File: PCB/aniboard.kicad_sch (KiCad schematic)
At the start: 368 parts, among them J1 Conn_02x03_Top_Bottom, SW1 SW_Push, SW10 SW_Push, SW11 SW_Push, SW12 SW_Push, SW13 SW_Push, SW14 SW_Push, SW15 SW_Push, SW16 SW_Push, SW17 SW_Push, SW18 SW_Push, SW19 SW_Push, SW2 SW_Push, SW20 SW_Push, SW21 SW_Push, SW22 SW_Push, SW23 SW_Push, SW24 SW_Push, SW25 SW_Push, SW26 SW_Push, SW27 SW_Push, SW28 SW_Push, SW29 SW_Push, SW3 SW_Push, SW30 SW_Push, SW31 SW_Push, SW32 SW_Push, SW33 SW_Push, SW34 SW_Push, SW35 SW_Push, SW36 SW_Push, SW37 SW_Push, SW38 SW_Push, SW39 SW_Push, SW4 SW_Push, SW40 SW_Push, SW41 SW_Push, SW42 SW_Push, SW43 SW_Push, SW44 SW_Push, SW45 SW_Push, SW46 SW_Push, SW47 SW_Push, SW48 SW_Push, SW49 SW_Push, SW5 SW_Push, SW50 SW_Push, SW51 SW_Push, SW52 SW_Push, SW53 SW_Push, SW54 SW_Push, SW55 SW_Push, SW56 SW_Push, SW57 SW_Push, SW58 SW_Push, SW59 SW_Push, SW6 SW_Push, SW60 SW_Push, SW61 SW_Push, SW62 SW_Push, SW63 SW_Push, SW64 SW_Push, SW65 SW_Push, SW66 SW_Push, SW67 SW_Push, SW68 SW_Push, SW69 SW_Push, SW7 SW_Push, SW70 SW_Push, SW71 SW_Push, SW72 SW_Push, SW73 SW_Push, SW74 SW_Push, SW75 SW_Push, SW76 SW_Push, SW77 SW_Push, SW78 SW_Push, SW79 SW_Push, SW8 SW_Push, SW80 SW_Push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

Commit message: Half done with routing
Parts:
- removed JP1: SolderJumper_2_Bridged, Jumper:SolderJumper-2_P1.3mm_Bridged_RoundedPad1.0x1.5mm, symbol Jumper:SolderJumper_2_Bridged
- removed JP2: SolderJumper_2_Open, Jumper:SolderJumper-2_P1.3mm_Open_RoundedPad1.0x1.5mm, symbol Jumper:SolderJumper_2_Open
- added C91, C92: 0.1uf, Capacitor_SMD:C_0805_2012Metric_Pad1.18x1.45mm_HandSolder, symbol Device:C_Small
- added R2: 470Ω, Resistor_SMD:R_0805_2012Metric_Pad1.20x1.40mm_HandSolder, symbol Device:R
- added R3: 100Ω, Resistor_SMD:R_0805_2012Metric_Pad1.20x1.40mm_HandSolder, symbol Device:R
- D89: value LED -> Blue LED; footprint (none) -> LED_SMD:LED_0603_1608Metric_Pad1.05x0.95mm_HandSolder
- D90: value LED -> Green LED; footprint (none) -> LED_SMD:LED_0603_1608Metric_Pad1.05x0.95mm_HandSolder
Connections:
- net +3.3V: now also U2.6 (VCCB), C91.2; no longer U2.1 (VCCA), U2.5 (DIR)
- net +5V: now also U1.39 (VSYS), U1.40 (VBUS), U2.1 (VCCA), C92.1, R2.1; no longer U2.6 (VCCB)
- net COL0: now also U1.21 (GPIO16); no longer U1.34 (GPIO28_ADC2)
- net COL1: now also U1.22 (GPIO17); no longer U1.32 (GPIO27_ADC1)
- net COL10: now also U1.17 (GPIO13); no longer U1.14 (GPIO10)
- net COL11: now also U1.19 (GPIO14); no longer U1.15 (GPIO11)
- net COL12: now also U1.15 (GPIO11); no longer U1.16 (GPIO12)
- net COL13: now also U1.14 (GPIO10)
- net COL14: now also U1.12 (GPIO9); no longer U1.10 (GPIO7)
- net COL15: now also U1.11 (GPIO8); no longer U1.9 (GPIO6)
- net COL16: now also U1.7 (GPIO5); no longer U1.5 (GPIO3)
- net COL2: now also U1.24 (GPIO18); no longer U1.22 (GPIO17)
- net COL3: now also U1.25 (GPIO19); no longer U1.20 (GPIO15)
- net COL4: now also U1.26 (GPIO20)
- net COL5: now also U1.27 (GPIO21)
- net COL6: now also U1.29 (GPIO22)
- net COL7: now also U1.31 (GPIO26_ADC0)
- net COL8: now also U1.32 (GPIO27_ADC1); no longer U1.11 (GPIO8)
- net COL9: now also U1.16 (GPIO12); no longer U1.12 (GPIO9)
- net GND: now also D89.1 (K), D90.1 (K), U2.5 (DIR), C91.1, C92.2; no longer U1.23 (GND)
- net LED: now also U1.34 (GPIO28_ADC2), U2.4 (B); no longer U1.21 (GPIO16), U2.3 (A)
- net ROW0: now also U1.20 (GPIO15); no longer U1.31 (GPIO26_ADC0)
- net ROW4: now also U1.10 (GPIO7); no longer U1.7 (GPIO5)
- net ROW5: now also U1.9 (GPIO6); no longer U1.6 (GPIO4)
- net RX: now also U1.6 (GPIO4)
- net TX: now also U1.5 (GPIO3)
- net at JP3.1 (A), R1.2: now also U2.3 (A); no longer U2.4 (B)
- net at D90.2 (A): now also R3.2
- net at D89.2 (A): now also R2.2
- new net INDICATOR: R3.1
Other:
- note added: "Indicator LEDs"
- moved on the sheet: D89, D90, U2

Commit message: Finish routing
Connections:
- net ROW0 is gone; now on net INDICATOR: D1.1 (K), D10.1 (K), D11.1 (K), D12.1 (K), D13.1 (K), D14.1 (K), D2.1 (K), D3.1 (K), D4.1 (K), D5.1 (K), D6.1 (K), D7.1 (K), D8.1 (K), D9.1 (K), U1.20 (GPIO15)
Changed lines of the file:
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@@
+		)
+	)
+	(global_label "INDICATOR"
+		(shape input)
+		(at 410.21 223.52 270)
+		(fields_autoplaced yes)
+		(effects
+			(font
+				(size 1.27 1.27)
+			)
+			(justify right)
+		)
+		(property "Intersheetrefs" "${INTERSHEET_REFS}"
+			(at 410.21 236.242 90)
+			(effects
+				(font
+					(size 1.27 1.27)
+				)
+				(justify right)
+				(hide yes)
+			)
 		)
 	)

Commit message: V1.2
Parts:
- removed J1: Conn_02x03_Top_Bottom, Connector_PinHeader_2.54mm:PinHeader_2x03_P2.54mm_Vertical, symbol Connector_Generic:Conn_02x03_Top_Bottom
- added Brd1: SSD1306, OLED:SSD1306-0.91-OLED-4pin-128x32, symbol OLED:SSD1306
- added C93: 1uf, Capacitor_SMD:C_0805_2012Metric_Pad1.18x1.45mm_HandSolder, symbol Device:C_Small
- added H1: MountingHole_Pad, MountingHole:MountingHole_3.2mm_M3_Pad_Via, symbol Mechanical:MountingHole_Pad
- added J2: Conn_01x03_Pin, Connector_PinHeader_2.54mm:PinHeader_1x03_P2.54mm_Vertical, symbol Connector:Conn_01x03_Pin
- added R4, R5: 4.7kΩ, Resistor_SMD:R_0805_2012Metric_Pad1.20x1.40mm_HandSolder, symbol Device:R
- C89, C90: value 500uf -> 5uf; footprint Capacitor_THT:CP_Radial_D8.0mm_P3.50mm -> Capacitor_THT:CP_Radial_D6.3mm_P2.50mm
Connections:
- net TX is gone; now on net COL16: U1.5 (GPIO3)
- net +3.3V: now also R4.1, R5.1
- net +5V: now also Brd1.2 (VCC), C93.2
- net COL10: now also U1.16 (GPIO12); no longer U1.17 (GPIO13)
- net COL11: now also U1.17 (GPIO13); no longer U1.19 (GPIO14)
- net COL12: now also U1.19 (GPIO14); no longer U1.15 (GPIO11)
- net COL16: no longer U1.7 (GPIO5)
- net COL9: now also U1.15 (GPIO11); no longer U1.16 (GPIO12)
- net GND: now also U1.23 (GND), Brd1.1 (GND), C93.1, H1.1, J2.2 (Pin_2)
- net at U1.41 (SWCLK): now also J2.1 (Pin_1)
- net at U1.43 (SWDIO): now also J2.3 (Pin_3)
- net RX: no longer names the net of U1.6 (GPIO4)
- net RX: now also Brd1.4 (SDA), R5.2
- new net: Brd1.3 (SCL), R4.2, U1.7 (GPIO5)

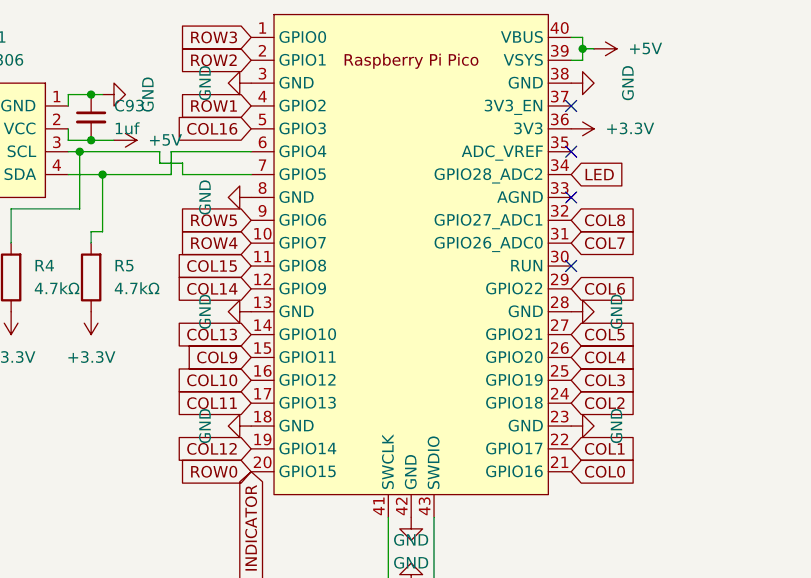
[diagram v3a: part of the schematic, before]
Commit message: Reroute and silkscreen
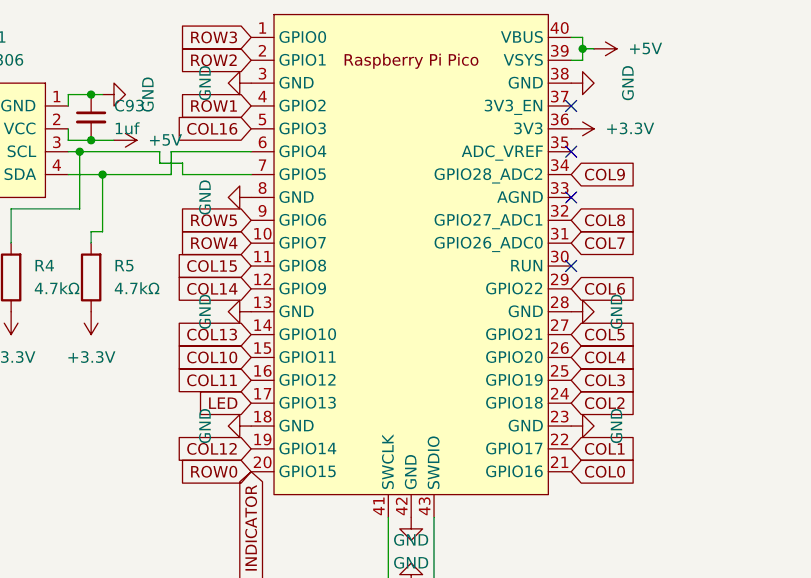
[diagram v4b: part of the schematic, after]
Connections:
- net COL10: now also U1.15 (GPIO11); no longer U1.16 (GPIO12)
- net COL11: now also U1.16 (GPIO12); no longer U1.17 (GPIO13)
- net COL9: now also U1.34 (GPIO28_ADC2); no longer U1.15 (GPIO11)
- net LED: now also U1.17 (GPIO13); no longer U1.34 (GPIO28_ADC2)

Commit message: Last pass
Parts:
- removed H1: MountingHole_Pad, MountingHole:MountingHole_3.2mm_M3_Pad_Via, symbol Mechanical:MountingHole_Pad
- D1, D10, D11, D12, D13, D14, D15, D16, D17, D18, D19, D2, D20, D21, D22, D23, D24, D25, D26, D27, D28, D29, D3, D30, D31, D32, D33, D34, D35, D36, D37, D38, D39, D4, D40, D41, D42, D43, D44, D45, D46, D47, D48, D49, D5, D50, D51, D52, D53, D54, D55, D56, D57, D58, D59, D6, D60, D61, D62, D63, D64, D65, D66, D67, D68, D69, D7, D70, D71, D72, D73, D74, D75, D76, D77, D78, D79, D8, D80, D81, D82, D83, D84, D85, D86, D87, D88, D9: footprint Diode_SMD:D_MiniMELF_Handsoldering -> Library:D_MiniMELF_Handsoldering

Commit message: Save
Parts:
- added J1, J2: USB_C_Receptacle_PowerOnly_24P, Connector_USB:USB_C_Receptacle_GCT_USB4135-GF-A_6P_TopMnt_Horizontal, symbol Connector:USB_C_Receptacle_PowerOnly_24P
- added J3, J4: Conn_01x02_Pin, Connector_PinHeader_2.54mm:PinHeader_1x02_P2.54mm_Vertical, symbol Connector:Conn_01x02_Pin
- added R6, R7, R8, R9: 5.1kΩ, Resistor_SMD:R_0805_2012Metric_Pad1.20x1.40mm_HandSolder, symbol Device:R
- C89, C90: value 5uf -> 4.7uf
- renumbered J2 to J5
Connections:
- net +5V: no longer C15.1, C16.1, C17.1, C18.1, C19.1, C20.1, C21.1, C22.1, C23.1, C24.1, C25.1, C26.1, C27.1, C28.1, C29.1, C30.1, C31.1, C32.1, C33.1, C34.1, C35.1, C36.1, C37.1, C38.1, C39.1, C40.1, C41.1, C42.1, C43.1, C44.1, C45.1, C46.1, C47.1, C48.1, C49.1, C50.1, C51.1, C52.1, C53.1, C54.1, C55.1, C56.1, C57.1, C58.1, C59.1, C60.1, C61.1, C62.1, C63.1, C64.1, C65.1, C66.1, C67.1, C68.1, C69.1, C70.1, C71.1, C72.1, C73.1, C74.1, C75.1, C76.1, C77.1, C78.1, C79.1, C80.1, C81.1, C82.1, C83.1, C84.1, C85.1, C86.1, C87.1, C88.1, LED15.1 (VDD), LED16.1 (VDD), LED17.1 (VDD), LED18.1 (VDD), LED19.1 (VDD), LED20.1 (VDD), LED21.1 (VDD), LED22.1 (VDD), LED23.1 (VDD), LED24.1 (VDD), LED25.1 (VDD), LED26.1 (VDD), LED27.1 (VDD), LED28.1 (VDD), LED29.1 (VDD), LED30.1 (VDD), LED31.1 (VDD), LED32.1 (VDD), LED33.1 (VDD), LED34.1 (VDD), LED35.1 (VDD), LED36.1 (VDD), LED37.1 (VDD), LED38.1 (VDD), LED39.1 (VDD), LED40.1 (VDD), LED41.1 (VDD), LED42.1 (VDD), LED43.1 (VDD), LED44.1 (VDD), LED45.1 (VDD), LED46.1 (VDD), LED47.1 (VDD), LED48.1 (VDD), LED49.1 (VDD), LED50.1 (VDD), LED51.1 (VDD), LED52.1 (VDD), LED53.1 (VDD), LED54.1 (VDD), LED55.1 (VDD), LED56.1 (VDD), LED57.1 (VDD), LED58.1 (VDD), LED59.1 (VDD), LED60.1 (VDD), LED61.1 (VDD), LED62.1 (VDD), LED63.1 (VDD), LED64.1 (VDD), LED65.1 (VDD), LED66.1 (VDD), LED67.1 (VDD), LED68.1 (VDD), LED69.1 (VDD), LED70.1 (VDD), LED71.1 (VDD), LED72.1 (VDD), LED73.1 (VDD), LED74.1 (VDD), LED75.1 (VDD), LED76.1 (VDD), LED77.1 (VDD), LED78.1 (VDD), LED79.1 (VDD), LED80.1 (VDD), LED81.1 (VDD), LED82.1 (VDD), LED83.1 (VDD), LED84.1 (VDD), LED85.1 (VDD), LED86.1 (VDD), LED87.1 (VDD), LED88.1 (VDD)
- net GND: now also J1.A1 (GND), J1.A12 (GND), J1.B1 (GND), J1.B12 (GND), J2.A1 (GND), J2.A12 (GND), J2.B1 (GND), J2.B12 (GND), J3.2 (Pin_2), J4.2 (Pin_2), R6.2, R7.2, R8.2, R9.2
- net INDICATOR renamed ROW0
- new net: J2.A5 (CC1), R8.1
- new net: J2.B5 (CC2), R9.1
- new net: J1.A5 (CC1), R6.1
- new net: J1.B5 (CC2), R7.1
- new net +5VA: C15.1, C16.1, C17.1, C18.1, C19.1, C20.1, C21.1, C22.1, C23.1, C24.1, C25.1, C26.1, C27.1, C28.1, C29.1, C30.1, C31.1, C32.1, C33.1, C34.1, C35.1, C36.1, C37.1, C38.1, C39.1, C40.1, C41.1, C42.1, C80.1, C81.1, C82.1, C83.1, C84.1, C85.1, J1.A4 (VBUS), J1.A9 (VBUS), J1.B4 (VBUS), J1.B9 (VBUS), J3.1 (Pin_1), LED15.1 (VDD), LED16.1 (VDD), LED17.1 (VDD), LED18.1 (VDD), LED19.1 (VDD), LED20.1 (VDD), LED21.1 (VDD), LED22.1 (VDD), LED23.1 (VDD), LED24.1 (VDD), LED25.1 (VDD), LED26.1 (VDD), LED27.1 (VDD), LED28.1 (VDD), LED29.1 (VDD), LED30.1 (VDD), LED31.1 (VDD), LED32.1 (VDD), LED33.1 (VDD), LED34.1 (VDD), LED35.1 (VDD), LED36.1 (VDD), LED37.1 (VDD), LED38.1 (VDD), LED39.1 (VDD), LED40.1 (VDD), LED41.1 (VDD), LED42.1 (VDD), LED80.1 (VDD), LED81.1 (VDD), LED82.1 (VDD), LED83.1 (VDD), LED84.1 (VDD), LED85.1 (VDD)
- new net +5VB: C43.1, C44.1, C45.1, C46.1, C47.1, C48.1, C49.1, C50.1, C51.1, C52.1, C53.1, C54.1, C55.1, C56.1, C57.1, C58.1, C59.1, C60.1, C61.1, C62.1, C63.1, C64.1, C65.1, C66.1, C67.1, C68.1, C69.1, C70.1, C71.1, C72.1, C73.1, C74.1, C75.1, C76.1, C77.1, C78.1, C79.1, C86.1, C87.1, C88.1, J2.A4 (VBUS), J2.A9 (VBUS), J2.B4 (VBUS), J2.B9 (VBUS), J4.1 (Pin_1), LED43.1 (VDD), LED44.1 (VDD), LED45.1 (VDD), LED46.1 (VDD), LED47.1 (VDD), LED48.1 (VDD), LED49.1 (VDD), LED50.1 (VDD), LED51.1 (VDD), LED52.1 (VDD), LED53.1 (VDD), LED54.1 (VDD), LED55.1 (VDD), LED56.1 (VDD), LED57.1 (VDD), LED58.1 (VDD), LED59.1 (VDD), LED60.1 (VDD), LED61.1 (VDD), LED62.1 (VDD), LED63.1 (VDD), LED64.1 (VDD), LED65.1 (VDD), LED66.1 (VDD), LED67.1 (VDD), LED68.1 (VDD), LED69.1 (VDD), LED70.1 (VDD), LED71.1 (VDD), LED72.1 (VDD), LED73.1 (VDD), LED74.1 (VDD), LED75.1 (VDD), LED76.1 (VDD), LED77.1 (VDD), LED78.1 (VDD), LED79.1 (VDD), LED86.1 (VDD), LED87.1 (VDD), LED88.1 (VDD)
- no-connect marks 5 -> 7

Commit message: Dual USB powah
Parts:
- removed J2: USB_C_Receptacle_PowerOnly_24P, Connector_USB:USB_C_Receptacle_GCT_USB4135-GF-A_6P_TopMnt_Horizontal, symbol Connector:USB_C_Receptacle_PowerOnly_24P
- removed R8: 5.1kΩ, Resistor_SMD:R_0805_2012Metric_Pad1.20x1.40mm_HandSolder, symbol Device:R
- added C100, C105, C36, C72: 10nF, Capacitor_SMD:C_0402_1005Metric_Pad0.74x0.62mm_HandSolder, symbol Device:C
- added C101, C106, C37, C73: 400pF, Capacitor_SMD:C_0402_1005Metric_Pad0.74x0.62mm_HandSolder, symbol Device:C
- added C104, C18, C55, C98: 0.1uF, Capacitor_SMD:C_0402_1005Metric_Pad0.74x0.62mm_HandSolder, symbol Device:C
- added C17: 4.7uf, Capacitor_THT:CP_Radial_D6.3mm_P2.50mm, symbol Device:C_Polarized
- added D15, D66, D91, D92: LED, LED_SMD:LED_0603_1608Metric_Pad1.05x0.95mm_HandSolder, symbol Device:LED
- added J3: USB_C_Receptacle_PowerOnly_24P, Connector_USB:USB_C_Receptacle_GCT_USB4135-GF-A_6P_TopMnt_Horizontal, symbol Connector:USB_C_Receptacle_PowerOnly_24P
- added JP1, JP3: Jumper_2_Open, Jumper:SolderJumper-2_P1.3mm_Open_RoundedPad1.0x1.5mm, symbol Jumper:Jumper_2_Open
- added P1, P2, P3, P4: ~, Library:TPS25947xx, symbol Library:TPS25947xx
- added R1, R15, R16, R18, R19, R2, R35, R36: 4.7kΩ, Resistor_SMD:R_0402_1005Metric_Pad0.72x0.64mm_HandSolder, symbol Device:R
- added R10, R14, R28, R34: 220Ω, Resistor_SMD:R_0402_1005Metric_Pad0.72x0.64mm_HandSolder, symbol Device:R
- added R11, R17, R29, R37: 1kΩ, Resistor_SMD:R_0402_1005Metric_Pad0.72x0.64mm_HandSolder, symbol Device:R
- added R12, R13, R20, R23, R26, R3, R32, R33, R6: 10kΩ, Resistor_SMD:R_0402_1005Metric_Pad0.72x0.64mm_HandSolder, symbol Device:R
- added R21, R22, R4, R5: 100kΩ, Resistor_SMD:R_0402_1005Metric_Pad0.72x0.64mm_HandSolder, symbol Device:R
- added R24, R25: 5.1kΩ, Resistor_SMD:R_0805_2012Metric_Pad1.20x1.40mm_HandSolder, symbol Device:R
- D93: renamed from D89; value Blue LED -> LED
- D94: renamed from D90; value Green LED -> LED
- R39: renamed from R3; value 100Ω -> 470Ω
- R9: value 5.1kΩ -> 10kΩ; footprint Resistor_SMD:R_0805_2012Metric_Pad1.20x1.40mm_HandSolder -> Resistor_SMD:R_0402_1005Metric_Pad0.72x0.64mm_HandSolder
- S5: footprint PCM_marbastlib-mx:STAB_MX_6.25u -> PCM_marbastlib-mx:STAB_MX_P_6.25u
- renumbered C92 to C102, C91 to C103, C89 to C15, C90 to C16, C15 to C19, C16 to C20, C17 to C21, C18 to C22, C19 to C23, C20 to C24, C21 to C25, C22 to C26, C23 to C27, C24 to C28, C25 to C29, C26 to C30, C27 to C31, C28 to C32, C80 to C33, C81 to C34, C82 to C35, C29 to C38, C30 to C39, C31 to C40, C32 to C41, C33 to C42, C34 to C43, C35 to C44, C36 to C45, C37 to C46, C38 to C47, C39 to C48, C40 to C49, C41 to C50, C42 to C51, C83 to C52, C84 to C53, C85 to C54, C43 to C56, C44 to C57, C45 to C58, C46 to C59, C47 to C60, C48 to C61, C49 to C62, C50 to C63, C51 to C64, C52 to C65, C53 to C66, C54 to C67, C55 to C68, C86 to C69, C87 to C70, C88 to C71, C56 to C74, C57 to C75, C58 to C76, C59 to C77, C60 to C78, C61 to C79, C62 to C80, C63 to C81, C64 to C82, C65 to C83, C66 to C84, C67 to C85, C79 to C86, C68 to C87, C69 to C88, C70 to C89, C71 to C90, C72 to C91, C73 to C92, C74 to C93, C75 to C94, C76 to C95, C77 to C96, C78 to C97, C93 to C99, D15 to D16, D16 to D17, D17 to D18, D18 to D19, D19 to D20, D20 to D21, D21 to D22, D22 to D23, D23 to D24, D24 to D25, D25 to D26, D26 to D27, D27 to D28, D28 to D29, D80 to D30, D81 to D31, D82 to D32, D29 to D33, D30 to D34, D31 to D35, D32 to D36, D33 to D37, D34 to D38, D35 to D39, D36 to D40, D37 to D41, D38 to D42, D39 to D43, D40 to D44, D41 to D45, D42 to D46, D83 to D47, D84 to D48, D85 to D49, D43 to D50, D44 to D51, D45 to D52, D46 to D53, D47 to D54, D48 to D55, D49 to D56, D50 to D57, D51 to D58, D52 to D59, D53 to D60, D54 to D61, D55 to D62, D86 to D63, D87 to D64, D88 to D65, D56 to D67, D57 to D68, D58 to D69, D59 to D70, D60 to D71, D61 to D72, D62 to D73, D63 to D74, D64 to D75, D65 to D76, D66 to D77, D67 to D78, D68 to D80, D69 to D81, D70 to D82, D71 to D83, D72 to D84, D73 to D85, D74 to D86, D75 to D87, D76 to D88, D77 to D89, D78 to D90, J3 to J2, JP3 to JP2, LED80 to LED29, LED81 to LED30, LED82 to LED31, LED29 to LED32, LED30 to LED33, LED31 to LED34, LED32 to LED35, LED33 to LED36, LED34 to LED37, LED35 to LED38, LED36 to LED39, LED37 to LED40, LED38 to LED41, LED39 to LED42, LED40 to LED43, LED41 to LED44, LED42 to LED45, LED83 to LED46, LED84 to LED47, LED85 to LED48, LED43 to LED49, LED44 to LED50, LED45 to LED51, LED46 to LED52, LED47 to LED53, LED48 to LED54, LED49 to LED55, LED50 to LED56, LED51 to LED57, LED52 to LED58, LED53 to LED59, LED54 to LED60, LED55 to LED61, LED86 to LED62, LED87 to LED63, LED88 to LED64, LED56 to LED65, LED57 to LED66, LED58 to LED67, LED59 to LED68, LED60 to LED69, LED61 to LED70, LED62 to LED71, LED63 to LED72, LED64 to LED73, LED65 to LED74, LED66 to LED75, LED67 to LED76, LED79 to LED77, LED68 to LED78, LED69 to LED79, LED70 to LED80, LED71 to LED81, LED72 to LED82, LED73 to LED83, LED74 to LED84, LED75 to LED85, LED76 to LED86, LED77 to LED87, LED78 to LED88, R1 to R27, R4 to R30, R5 to R31, R2 to R38, R6 to R7, R7 to R8, SW80 to SW29, SW81 to SW30, SW82 to SW31, SW29 to SW32, SW30 to SW33, SW31 to SW34, SW32 to SW35, SW33 to SW36, SW34 to SW37, SW35 to SW38, SW36 to SW39, SW37 to SW40, SW38 to SW41, SW39 to SW42, SW40 to SW43, SW41 to SW44, SW42 to SW45, SW83 to SW46, SW84 to SW47, SW85 to SW48, SW43 to SW49, SW44 to SW50, SW45 to SW51, SW46 to SW52, SW47 to SW53, SW48 to SW54, SW49 to SW55, SW50 to SW56, SW51 to SW57, SW52 to SW58, SW53 to SW59, SW54 to SW60, SW55 to SW61, SW86 to SW62, SW87 to SW63, SW88 to SW64, SW56 to SW65, SW57 to SW66, SW58 to SW67, SW59 to SW68, SW60 to SW69, SW61 to SW70, SW62 to SW71, SW63 to SW72, SW64 to SW73, SW65 to SW74, SW66 to SW75, SW67 to SW76, SW79 to SW77, SW68 to SW78, SW69 to SW79, SW70 to SW80, SW71 to SW81, SW72 to SW82, SW73 to SW83, SW74 to SW84, SW75 to SW85, SW76 to SW86, SW77 to SW87, SW78 to SW88, U2 to U1, U1 to U2
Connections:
- net +5V: now also C32.1, C33.1, C34.1, C35.1, C51.1, C52.1, C53.1, C54.1, C68.1, C69.1, C70.1, C71.1, C86.1, C94.1, C95.1, C96.1, C97.1, C99.1, LED28.1 (VDD), LED29.1 (VDD), LED30.1 (VDD), LED31.1 (VDD), LED45.1 (VDD), LED46.1 (VDD), LED47.1 (VDD), LED48.1 (VDD), LED61.1 (VDD), LED62.1 (VDD), LED63.1 (VDD), LED64.1 (VDD), LED77.1 (VDD), LED85.1 (VDD), LED86.1 (VDD), LED87.1 (VDD), LED88.1 (VDD), C104.1, C55.1, JP1.2 (B), JP3.2 (B), P2.5 (IN), P4.5 (IN), R12.1, R32.1; no longer C1.1, C10.1, C11.1, C12.1, C13.1, C16.1, C2.1, C3.1, C4.1, C5.1, C6.1, C7.1, C8.1, C9.1, C99.2, LED1.1 (VDD), LED10.1 (VDD), LED11.1 (VDD), LED12.1 (VDD), LED13.1 (VDD), LED2.1 (VDD), LED3.1 (VDD), LED4.1 (VDD), LED5.1 (VDD), LED6.1 (VDD), LED7.1 (VDD), LED8.1 (VDD), LED9.1 (VDD)
- net +5VA: now also C1.1, C16.1, C2.1, C3.1, C4.1, C5.1, C56.1, C57.1, C58.1, C59.1, C6.1, C60.1, C61.1, C74.1, C75.1, C76.1, C77.1, C78.1, C79.1, C80.1, C87.1, C88.1, C89.1, C90.1, LED1.1 (VDD), LED2.1 (VDD), LED3.1 (VDD), LED4.1 (VDD), LED49.1 (VDD), LED5.1 (VDD), LED50.1 (VDD), LED51.1 (VDD), LED52.1 (VDD), LED53.1 (VDD), LED54.1 (VDD), LED6.1 (VDD), LED65.1 (VDD), LED66.1 (VDD), LED67.1 (VDD), LED68.1 (VDD), LED69.1 (VDD), LED70.1 (VDD), LED71.1 (VDD), LED78.1 (VDD), LED79.1 (VDD), LED80.1 (VDD), LED81.1 (VDD), JP1.1 (A), P1.6 (OUT), P2.6 (OUT), R1.1, R15.1, R16.1, R2.1; no longer C25.1, C26.1, C27.1, C28.1, C29.1, C30.1, C31.1, C32.1, C33.1, C34.1, C35.1, C45.1, C46.1, C47.1, C48.1, C49.1, C50.1, C51.1, C52.1, C53.1, C54.1, J1.A4 (VBUS), J1.A9 (VBUS), J1.B4 (VBUS), J1.B9 (VBUS), J2.1 (Pin_1), LED21.1 (VDD), LED22.1 (VDD), LED23.1 (VDD), LED24.1 (VDD), LED25.1 (VDD), LED26.1 (VDD), LED27.1 (VDD), LED28.1 (VDD), LED29.1 (VDD), LED30.1 (VDD), LED31.1 (VDD), LED39.1 (VDD), LED40.1 (VDD), LED41.1 (VDD), LED42.1 (VDD), LED43.1 (VDD), LED44.1 (VDD), LED45.1 (VDD), LED46.1 (VDD), LED47.1 (VDD), LED48.1 (VDD)
- net +5VB: now also C10.1, C11.1, C12.1, C13.1, C25.1, C26.1, C27.1, C28.1, C29.1, C30.1, C31.1, C45.1, C46.1, C47.1, C48.1, C49.1, C50.1, C7.1, C8.1, C9.1, LED10.1 (VDD), LED11.1 (VDD), LED12.1 (VDD), LED13.1 (VDD), LED21.1 (VDD), LED22.1 (VDD), LED23.1 (VDD), LED24.1 (VDD), LED25.1 (VDD), LED26.1 (VDD), LED27.1 (VDD), LED39.1 (VDD), LED40.1 (VDD), LED41.1 (VDD), LED42.1 (VDD), LED43.1 (VDD), LED44.1 (VDD), LED7.1 (VDD), LED8.1 (VDD), LED9.1 (VDD), C17.1, JP3.1 (A), P3.6 (OUT), P4.6 (OUT), R18.1, R19.1, R35.1, R36.1; no longer C56.1, C57.1, C58.1, C59.1, C60.1, C61.1, C68.1, C69.1, C70.1, C71.1, C74.1, C75.1, C76.1, C77.1, C78.1, C79.1, C80.1, C86.1, C87.1, C88.1, C89.1, C90.1, C94.1, C95.1, C96.1, C97.1, J4.1 (Pin_1), LED49.1 (VDD), LED50.1 (VDD), LED51.1 (VDD), LED52.1 (VDD), LED53.1 (VDD), LED54.1 (VDD), LED61.1 (VDD), LED62.1 (VDD), LED63.1 (VDD), LED64.1 (VDD), LED65.1 (VDD), LED66.1 (VDD), LED67.1 (VDD), LED68.1 (VDD), LED69.1 (VDD), LED70.1 (VDD), LED71.1 (VDD), LED77.1 (VDD), LED78.1 (VDD), LED79.1 (VDD), LED80.1 (VDD), LED81.1 (VDD), LED85.1 (VDD), LED86.1 (VDD), LED87.1 (VDD), LED88.1 (VDD)
- net GND: now also C99.2, C100.2, C101.2, C104.2, C105.2, C106.2, C17.2, C18.2, C36.2, C37.2, C55.2, C72.2, C73.2, C98.2, D15.1 (K), D66.1 (K), D91.1 (K), D92.1 (K), J3.A1 (GND), J3.A12 (GND), J3.B1 (GND), J3.B12 (GND), P1.8 (GND), P2.8 (GND), P3.8 (GND), P4.8 (GND), R11.2, R13.2, R17.2, R23.2, R24.2, R25.2, R26.2, R29.2, R33.2, R37.2, R6.2; no longer C99.1
- net at R9.1: now also P1.2 (OVLO), R4.2, R5.2
- new net: C100.1, P3.10 (ITIMER)
- new net: J3.B5 (CC2), R25.1
- new net: P2.1 (EN/UVLO), R12.2, R13.1
- new net: C72.1, P2.10 (ITIMER)
- new net: P1.3 (AUXOFF), P2.2 (OVLO), R2.2
- new net: P2.3 (AUXOFF), R16.2
- new net: D66.2 (A), P2.4 (FLT), R15.2
- new net: C73.1, P2.7 (DVDT)
- new net: P2.9 (ILM), R14.1
- new net: P3.3 (AUXOFF), P4.2 (OVLO), R19.2
- new net: C98.1, J3.A4 (VBUS), J3.A9 (VBUS), J3.B4 (VBUS), J3.B9 (VBUS), J4.1 (Pin_1), P3.5 (IN), R20.1, R21.1, R22.1
- new net: P3.2 (OVLO), R21.2, R22.2, R26.1
- new net: D91.2 (A), P3.4 (FLT), R18.2
- new net: C18.1, J1.A4 (VBUS), J1.A9 (VBUS), J1.B4 (VBUS), J1.B9 (VBUS), J2.1 (Pin_1), P1.5 (IN), R3.1, R4.1, R5.1
- new net: P1.1 (EN/UVLO), R3.2, R6.1
- new net: R34.2, R37.1
- new net: J3.A5 (CC1), R24.1
- new net: R10.2, R11.1
- new net: R28.2, R29.1
- new net: P4.1 (EN/UVLO), R32.2, R33.1
- new net: P1.9 (ILM), R10.1
- new net: R14.2, R17.1
- new net: C105.1, P4.10 (ITIMER)
- new net: P4.3 (AUXOFF), R36.2
- new net: D92.2 (A), P4.4 (FLT), R35.2
- new net: C106.1, P4.7 (DVDT)
- new net: P4.9 (ILM), R34.1
- new net: P3.1 (EN/UVLO), R20.2, R23.1
- new net: C101.1, P3.7 (DVDT)
- new net: C36.1, P1.10 (ITIMER)
- new net: C37.1, P1.7 (DVDT)
- new net: D15.2 (A), P1.4 (FLT), R1.2
- new net: P3.9 (ILM), R28.1
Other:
- note added: "Dual USB-C power supply module"
- moved on the sheet: C1, C10, C11, C12, C13, C14, C15, C16, C19, C2, C20, C21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

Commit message: BOM
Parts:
- C15, C16, C17: footprint Capacitor_THT:CP_Radial_D6.3mm_P2.50mm -> Capacitor_SMD:C_0402_1005Metric_Pad0.74x0.62mm_HandSolder
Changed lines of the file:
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@@
 			)
 		)
-		(property "Footprint" "Capacitor_THT:CP_Radial_D6.3mm_P2.50mm"
+		(property "Footprint" "Capacitor_SMD:C_0402_1005Metric_Pad0.74x0.62mm_HandSolder"
 			(at 469.5952 33.02 0)
 			(effects
@@
 			)
 		)
-		(property "Footprint" "Capacitor_THT:CP_Radial_D6.3mm_P2.50mm"
+		(property "Footprint" "Capacitor_SMD:C_0402_1005Metric_Pad0.74x0.62mm_HandSolder"
 			(at 442.9252 33.02 0)
 			(effects
@@
 			)
 		)
-		(property "Footprint" "Capacitor_THT:CP_Radial_D6.3mm_P2.50mm"
+		(property "Footprint" "Capacitor_SMD:C_0402_1005Metric_Pad0.74x0.62mm_HandSolder"
 			(at 456.8952 33.02 0)
 			(effects
